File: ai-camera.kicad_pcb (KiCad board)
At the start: 4 copper layers, 70 x 70 mm, 174 parts, among them J1 Conn-01x02_P2mm_NONAME_JST-PH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, J2 TYPE-C-31-M-12, J3 DBG, J4 Conn-02x10_P2.54mm_B-2100S20P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, J5 Conn-01x02_P1.25mm_10114829-1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, J6 Conn_01x24_FFC_0.5mm_AFC01-S2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, Q1 AO3401A, Q2 AO3400A, Q3 AO3400A, Q4 AO3401A, Q5 AO3400A, Q6 AO3401A, Q7 AO3400A, Q8 AO3401A, Q9 AO3400A, SW1 SW_PB_90deg_K2-1102AQ-H4CW-01, SW2 SW_PB_TS-1187A-B-A-B, SW3 SW_PB_TS-1187A-B-A-B, SW4 SW_PB_90deg_K2-1102AQ-H4CW-01, U1 PCF8563T/5,518, U10 AP1511B, U11 ESP32-S3-WROOM-1-N16R8, U12 MT9284-28J, U13 APDS-9306-065, U2 TP4057-42-SOT26-R, U3 XC6206-2.8V, U4 SRV05-4, U5 SOT-23-6_SN74LVC1G373DBVR_TI, U6 SY8089AAAC, U7 PIR_AS312, U8 XC6206-2.8V, U9 RT9166-12GVL, Y1 32.768kHz_Q13FC1350000400

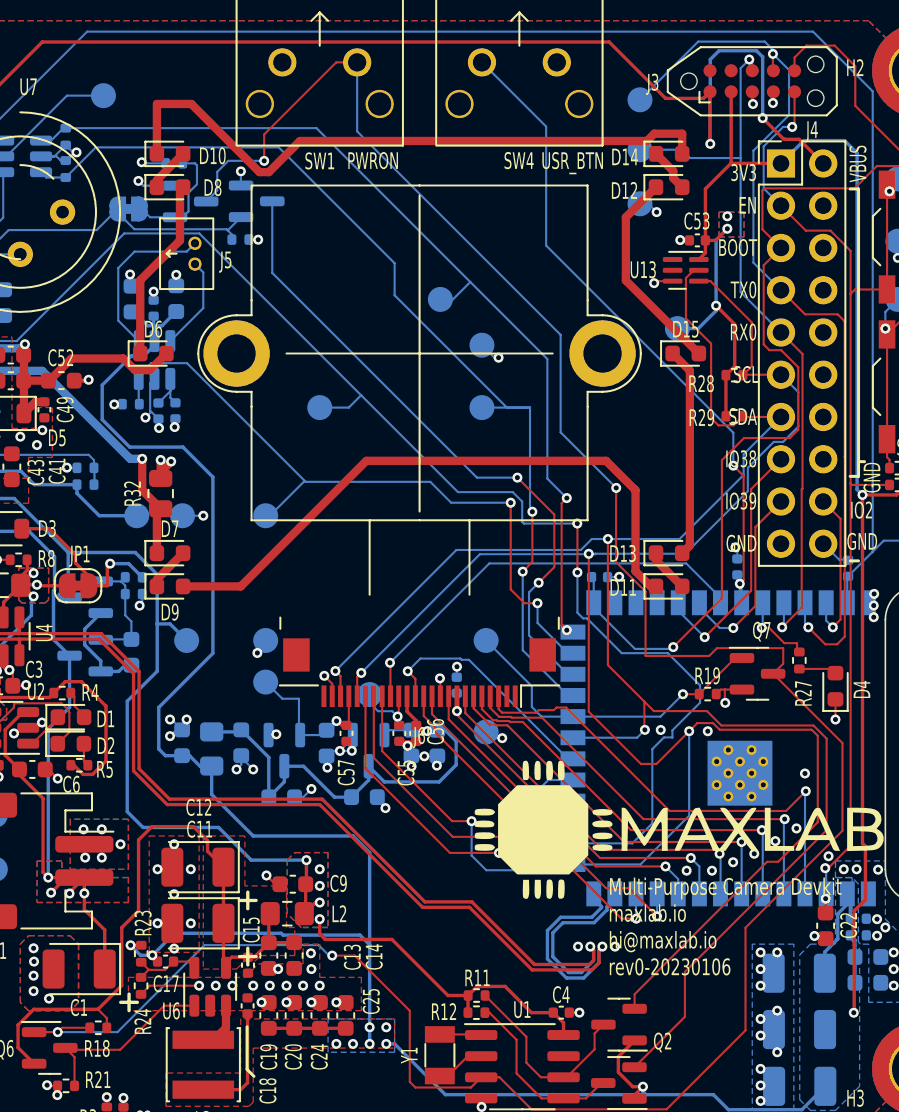
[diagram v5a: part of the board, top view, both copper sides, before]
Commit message: EAC-2: bot silkscreen fix
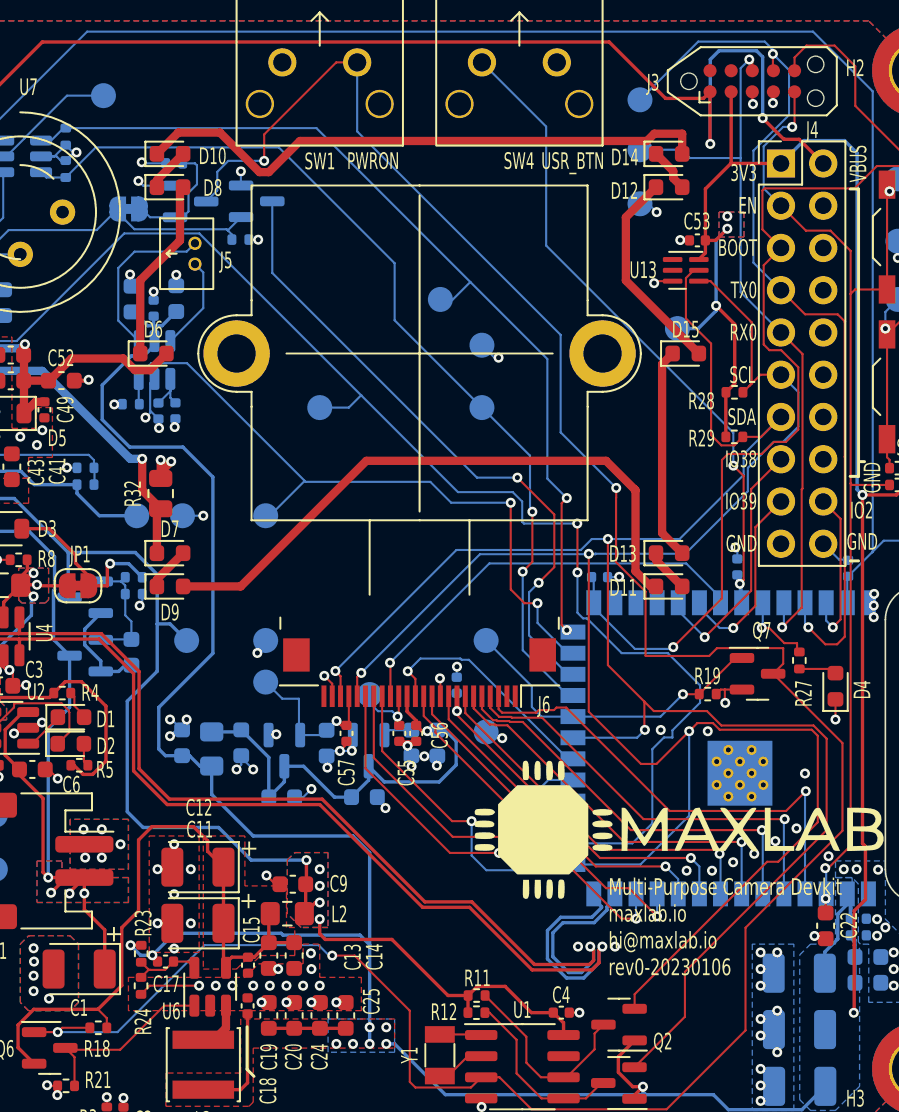
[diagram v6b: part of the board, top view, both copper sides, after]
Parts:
- moved R29 1.24 mm to (148.9, 72.0)
- moved R28 1.03 mm to (148.9, 69.3)
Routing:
- net /PIR_CTRL_D: track 59.5 -> 55.8 mm
- net Net-(D10-K): track 38.4 -> 35.3 mm
- net /CAM.SDA: track 103.0 -> 104.7 mm
- net +3V3: track 228.3 -> 229.5 mm
- net /CAM.SCL: track 109.1 -> 110.0 mm
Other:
- board text added: "locked"
- board text removed: "NOTES: Battery connector: JST-PH 2mm pitch IRCUT connector: MolexPicoblade 1.25mm pitch"

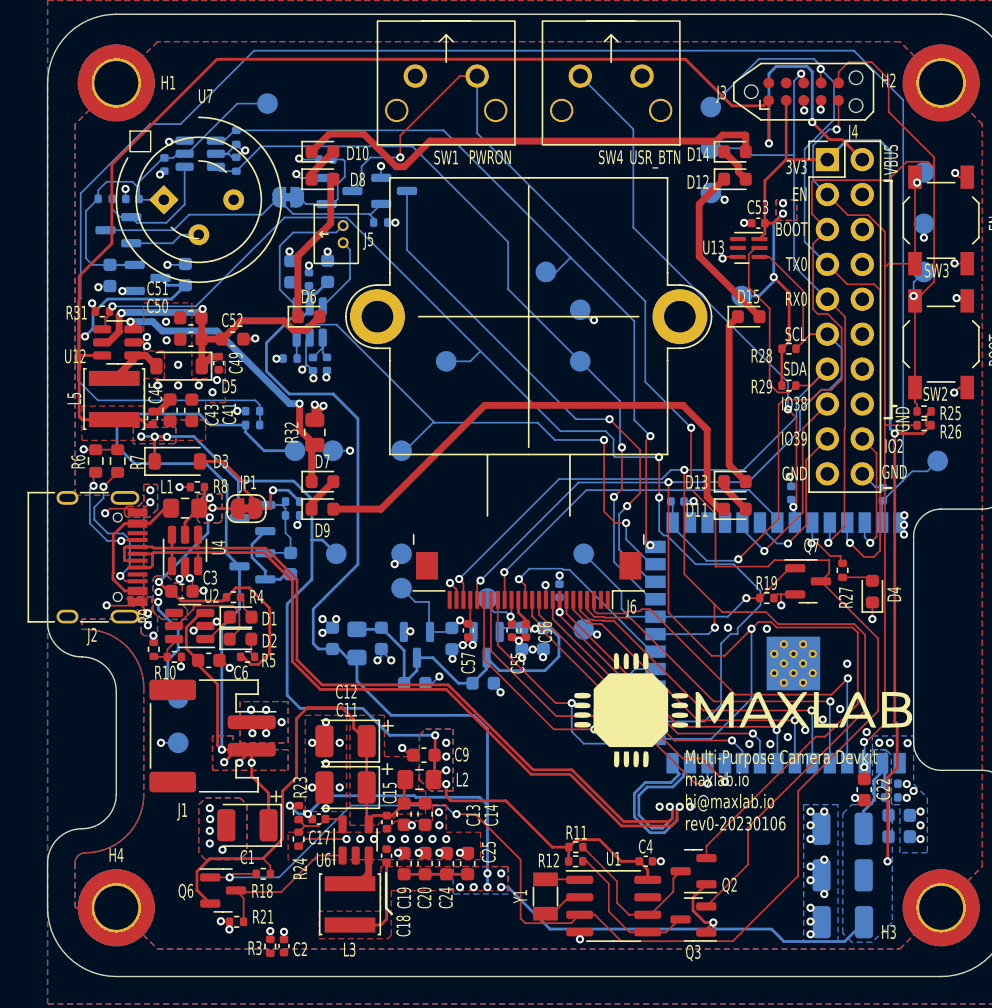
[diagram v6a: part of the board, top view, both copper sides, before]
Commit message: EAC-2: use discrete TVSs to avoid backfeeding the 5V line when USB is off
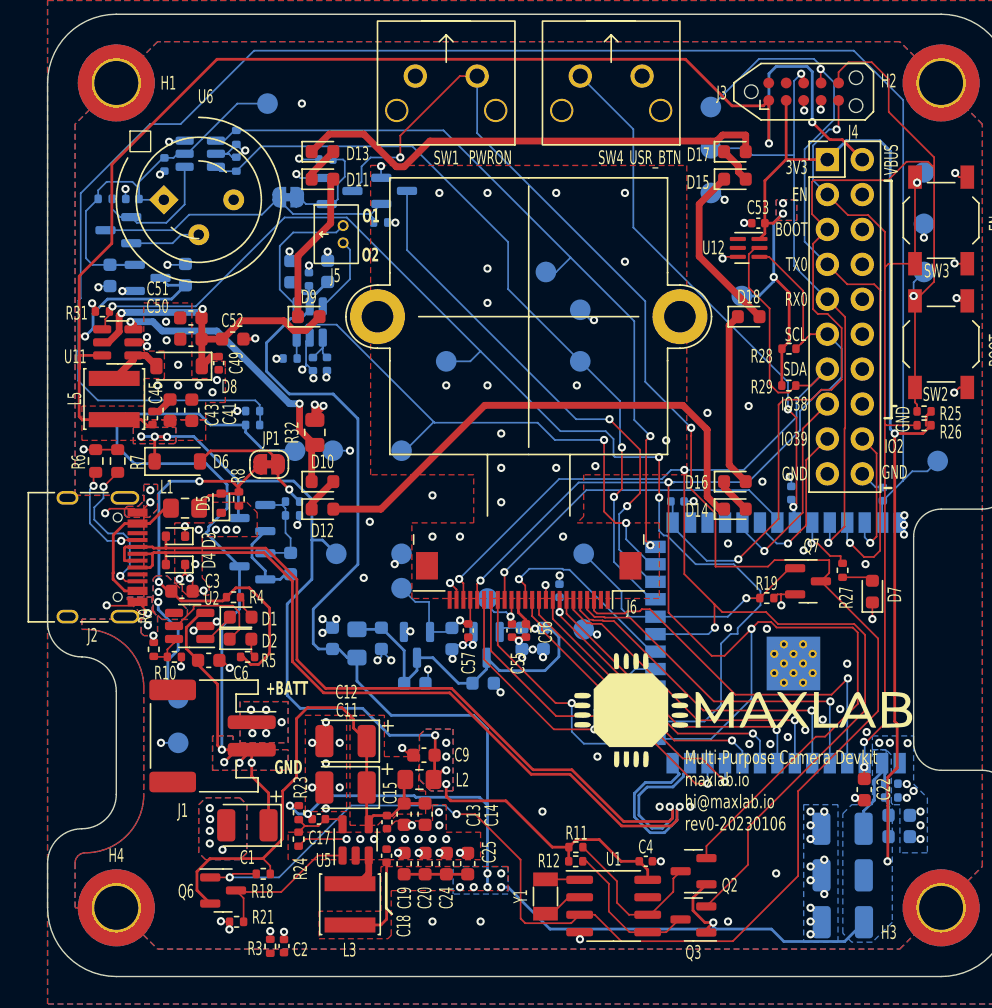
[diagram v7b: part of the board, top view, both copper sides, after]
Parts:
- removed the U4 at (105.0, 84.0)
- added D3: SOD-523_BSD5C051L, Diode_SMD:D_SOD-523, F.Cu at (104.3, 83.0)
- added D4: SOD-523_BSD5C051L, Diode_SMD:D_SOD-523, F.Cu at (104.3, 85.0)
- added D5: SOD-523_BSD5C051L, Diode_SMD:D_SOD-523, F.Cu at (107.6, 80.6)
- moved JP1 3.62 mm to (111.1, 77.7)
- moved R8 3.14 mm to (108.9, 80.3), turned to -90 degrees
- renumbered D7 to D10, D8 to D11, D9 to D12, D10 to D13, D11 to D14, D12 to D15, D13 to D16, D14 to D17, D15 to D18, D3 to D6, D4 to D7, D5 to D8, D6 to D9, U11 to U10, U12 to U11, U13 to U12, U5 to U4, U6 to U5, U7 to U6, U8 to U7, U9 to U8, U10 to U9
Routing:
- net +5V: track 38.2 -> 42.5 mm, vias 6 -> 4
- net +BATT: track 67.7 -> 68.9 mm
- net /UD-: track 66.6 -> 65.5 mm
- net /UD+: track 67.4 -> 66.3 mm
- net Net-(D6-A): track 10.3 -> 9.65 mm
- net GND: track 99.0 -> 98.5 mm, vias 162 -> 202
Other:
- board text added: "+BATT"
- board text added: "O1"
- board text added: "O2"
